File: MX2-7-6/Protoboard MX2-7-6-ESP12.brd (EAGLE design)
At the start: 54.4 x 59.6 mm, 52 parts, among them X1 ESP-12E

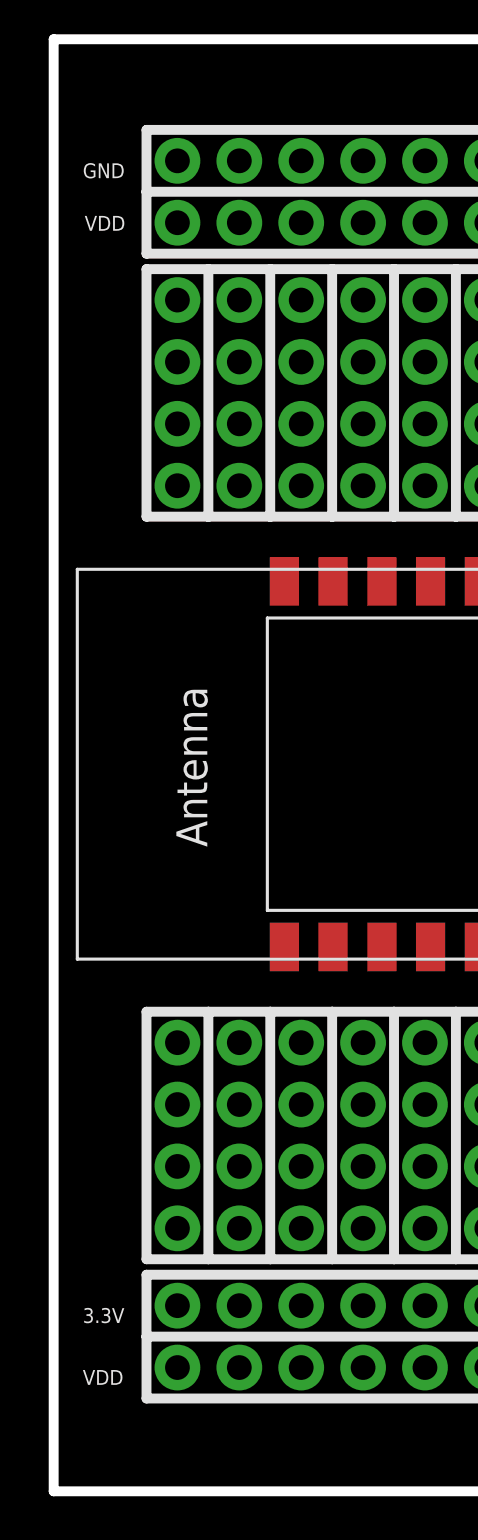
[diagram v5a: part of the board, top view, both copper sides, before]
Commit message: update and and 3.3V label
Update labels
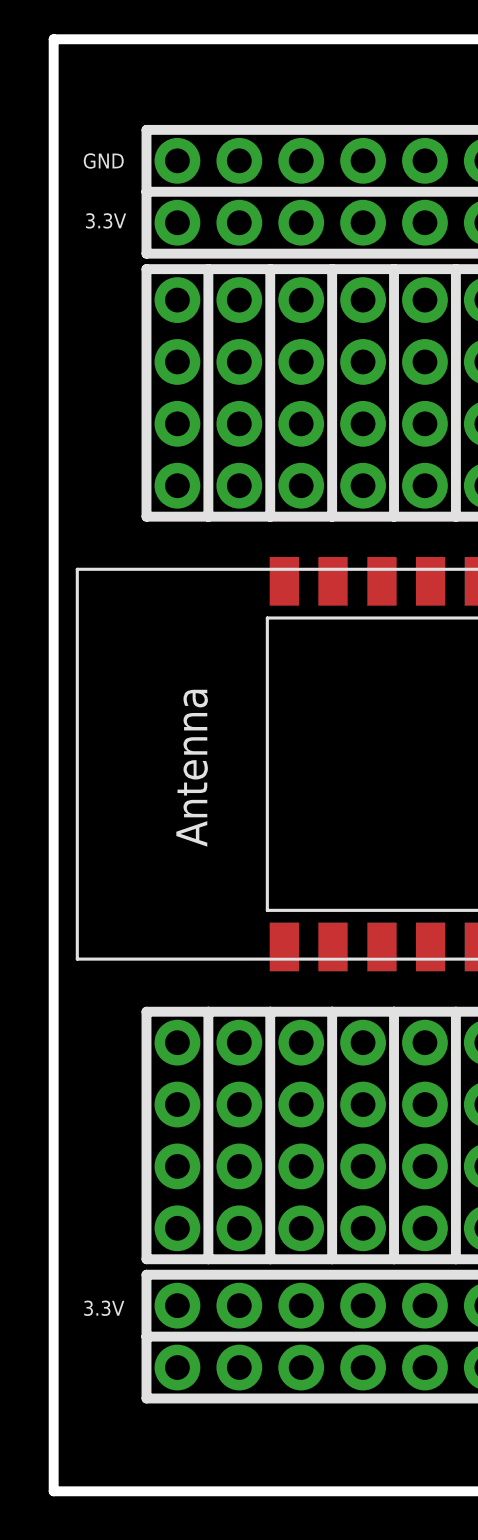
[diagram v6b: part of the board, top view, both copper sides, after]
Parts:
- VDD: value (none) -> GND
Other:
- board text added: "3.3V"
- board text removed: "VDD"
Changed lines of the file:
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@@
 <setting verticaltext="up"/>
 </settings>
-<grid distance="1.27" unitdist="mm" unit="mm" style="dots" multiple="1" display="yes" altdistance="25" altunitdist="mil" altunit="mm"/>
+<grid distance="1.27" unitdist="mm" unit="mm" style="dots" multiple="1" display="yes" altdistance="0.1" altunitdist="mm" altunit="mm"/>
 <layers>
 <layer number="1" name="Top" color="4" fill="1" visible="yes" active="yes"/>
@@
 <dimension x1="3.81" y1="3.81" x2="3.81" y2="0" x3="-7.62" y3="1.905" textsize="1.778" layer="47"/>
 <dimension x1="44.45" y1="54.61" x2="44.45" y2="59.69" x3="66.04" y3="57.15" textsize="1.778" layer="47"/>
-<text x="1.27" y="51.7398" size="0.6096" layer="25">VDD</text>
+<text x="1.27" y="51.8398" size="0.6096" layer="25">3.3V</text>
 <dimension x1="50.97" y1="50.165" x2="54.61" y2="50.165" x3="52.79" y3="50.165" textsize="1.778" layer="47"/>
 <wire x1="53.975" y1="52.705" x2="44.45" y2="52.705" width="0.4064" layer="25"/>
@@
 </element>
 <element name="GND" library="SparkFun-Connectors" package="1X16_NO_SILK" value="" x="5.08" y="54.61" smashed="yes">
-<attribute name="NAME" x="1.1938" y="53.8988" size="0.6096" layer="25" ratio="10"/>
+<attribute name="NAME" x="1.1938" y="54.2988" size="0.6096" layer="25" ratio="10"/>
 <attribute name="VALUE" x="3.81" y="51.435" size="1.27" layer="27"/>
 </element>
-<element name="VDD" library="SparkFun-Connectors" package="1X19_NO_SILK" value="" x="5.08" y="5.08" smashed="yes">
-<attribute name="NAME" x="1.1938" y="4.3688" size="0.6096" layer="25" ratio="10"/>
-<attribute name="VALUE" x="3.81" y="1.905" size="1.27" layer="27"/>
+<element name="VDD" library="SparkFun-Connectors" package="1X19_NO_SILK" value="GND" x="5.08" y="5.08" smashed="yes">
+<attribute name="VALUE" x="1.17" y="4.745" size="0.6096" layer="27"/>
 </element>
 <element name="3.3V" library="SparkFun-Connectors" package="1X19_NO_SILK" value="" x="5.08" y="7.62" smashed="yes">
-<attribute name="NAME" x="1.1938" y="6.9088" size="0.6096" layer="25" ratio="10"/>
+<attribute name="NAME" x="1.1938" y="7.2088" size="0.6096" layer="25" ratio="10"/>
 <attribute name="VALUE" x="3.81" y="4.445" size="1.27" layer="27"/>
 </element>

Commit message: Routed
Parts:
- moved J1 15.2 mm to (5.08, 41.3)
- moved J2 15.2 mm to (7.62, 41.3)
- moved J6 5.08 mm to (17.8, 41.3)
- moved J3 5.08 mm to (10.2, 41.3)
- moved J5 5.08 mm to (15.2, 41.3)
- moved J7 5.08 mm to (20.3, 41.3)
- moved J4 5.08 mm to (12.7, 41.3)
- moved J8 5.08 mm to (22.9, 41.3)
- moved JP5 3.05 mm to (27.3, 23.6)
- moved JP4 2.03 mm to (27.3, 31.2)
- moved JP3 2.03 mm to (27.3, 33.8)
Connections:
- removed net N$7: J1.1, J1.2, J1.3, J1.4
- removed net N$8: J2.1, J2.2, J2.3, J2.4
- net RX: now also J2.1, J2.2, J2.3, J2.4
- net TX: now also J1.1, J1.2, J1.3, J1.4
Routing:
- net VDD: track 0.00 -> 197.9 mm, vias 0 -> 1
- net TX: track 0.00 -> 35.2 mm, vias 0 -> 1
- net RX: track 0.00 -> 33.5 mm, vias 0 -> 1
- net VCC: track 0.00 -> 26.2 mm
- net N$28: track 0.00 -> 17.8 mm
- net N$27: track 0.00 -> 17.8 mm
- net N$25: track 0.00 -> 17.8 mm
- net N$22: track 0.00 -> 17.8 mm
- net N$50: track 0.00 -> 15.4 mm
- net N$21: track 0.00 -> 15.2 mm
- net N$20: track 0.00 -> 15.2 mm
- net N$19: track 0.00 -> 15.2 mm
- net N$18: track 0.00 -> 15.2 mm
- net N$17: track 0.00 -> 15.2 mm
- net N$1: track 0.00 -> 15.2 mm
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
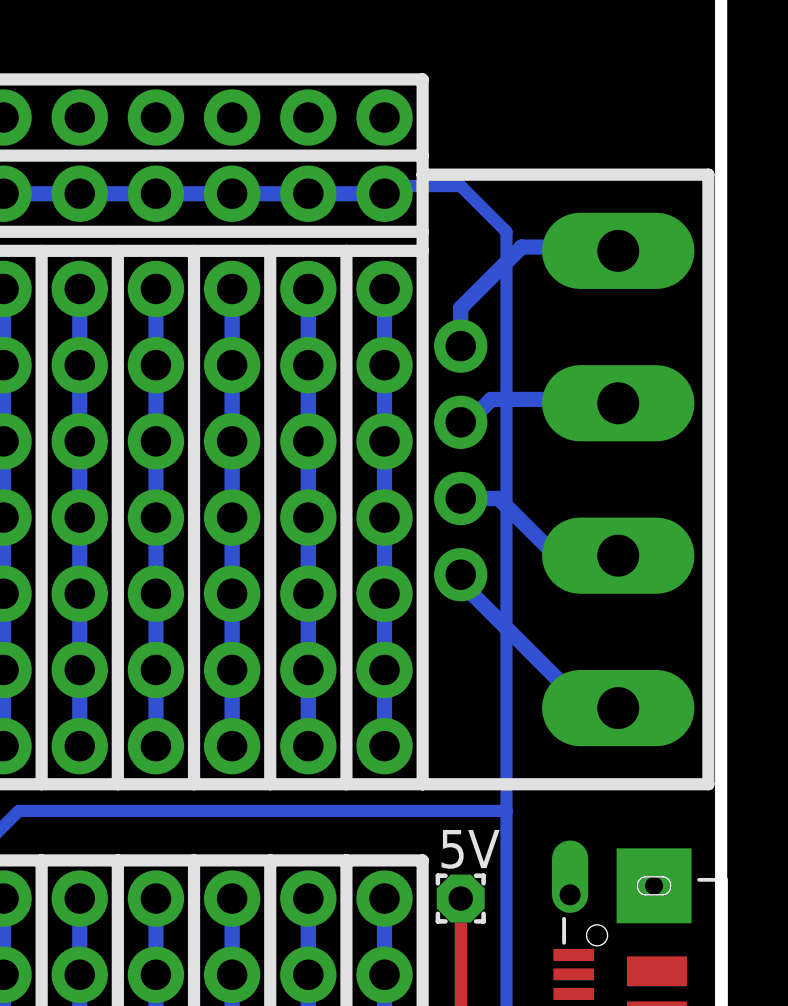
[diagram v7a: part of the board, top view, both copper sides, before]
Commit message: Crossing lines with 3.3V
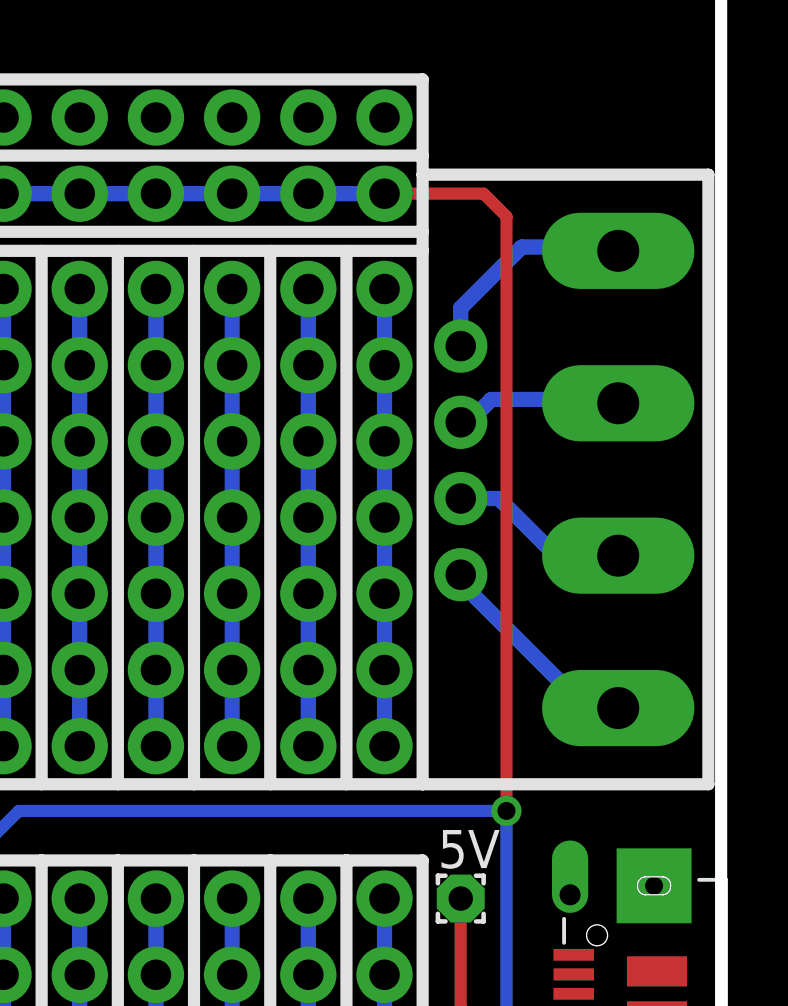
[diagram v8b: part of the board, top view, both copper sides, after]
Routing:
- net VDD: track 197.9 -> 198.0 mm, vias 1 -> 2
